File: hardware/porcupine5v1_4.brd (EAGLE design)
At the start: 28.5 x 29.7 mm, 45 parts, among them X1 PROGCON

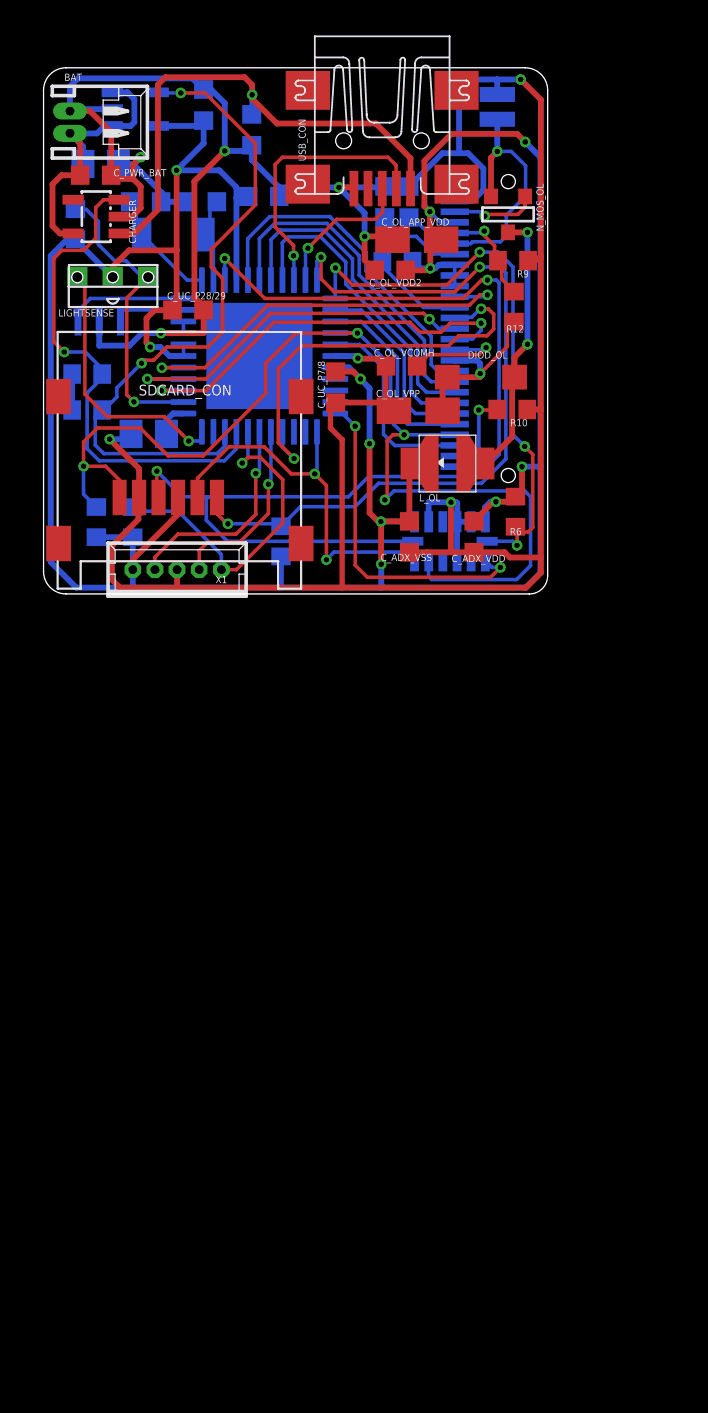
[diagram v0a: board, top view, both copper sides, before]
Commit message: added new OLEDdisplay
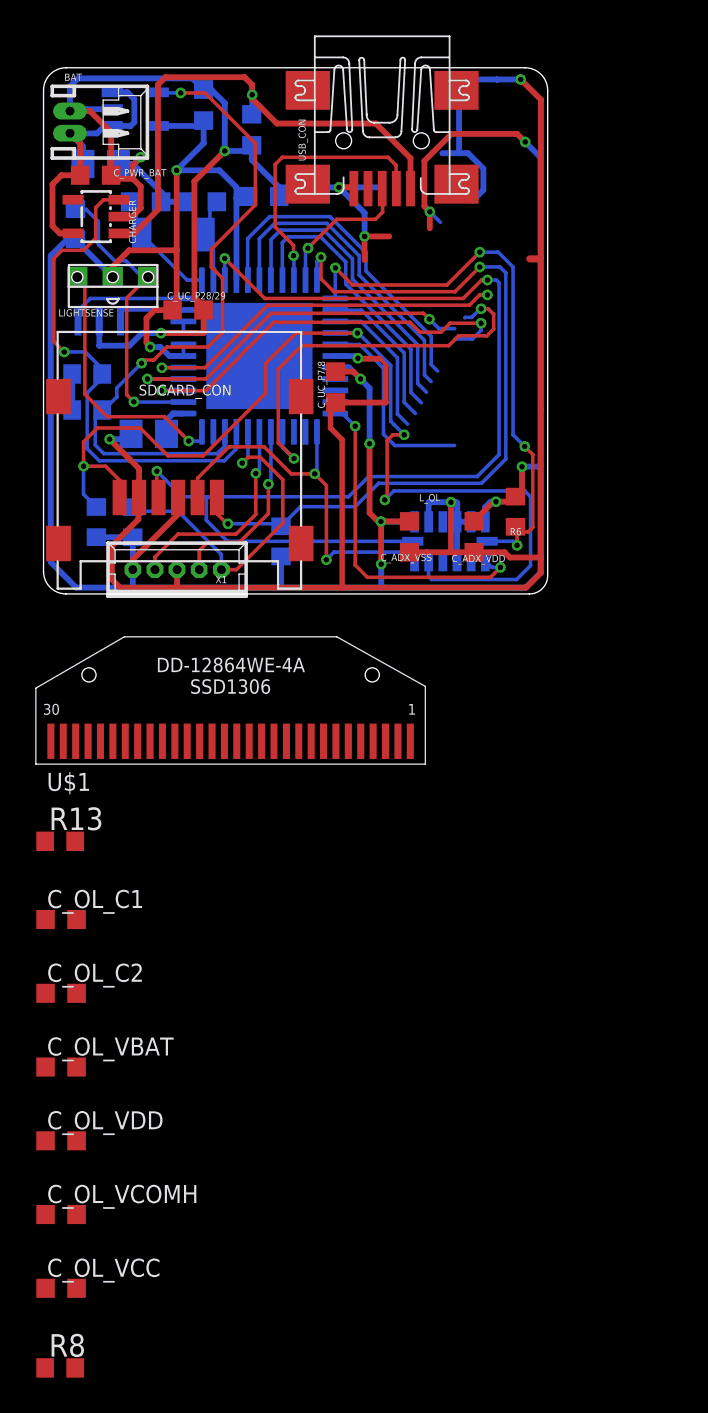
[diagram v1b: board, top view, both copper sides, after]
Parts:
- removed CON_OLED: OLED_DENSITRON, HedgehogLib:CON_DD-12864WE-1A
- removed C_OL_APP_VDD: 10µF/6.3V low ESR, rcl:A/3216-18R
- removed C_OL_FB: 1n, rcl:C0603K
- removed C_OL_VBREF: 1u, rcl:C0603K
- removed C_OL_VDD2: 1µF/16V, rcl:C0603K
- removed C_OL_VPP: 6.8µF/16V low ESR, rcl:A/3216-18R
- removed DIOD_OL: MBR0520, HedgehogLib:SOD123
- removed L_OL: 10µH, HedgehogLib:1212_FOR_INDUCTANCE
- removed N_MOS_OL: (no value), HedgehogLib:SOT-23
- removed R10: 820k, rcl:R0603
- removed R11, R12: 930k 1%, rcl:R0603
- removed R9: 110k 1%, rcl:R0603
- added C_OL_C1, C_OL_C2, C_OL_VBAT, C_OL_VDD: 1µF, rcl:C0603K
- added C_OL_VCC: 4.7µF, rcl:C0603K
- added R13: 400k, rcl:R0603
- added U$1: DD-12864WE-4A, HedgehogLib:CON_DD-12864WE-4A
- C_OL_VCOMH: value 4.7u -> 4.7µF
- R8: value 0.12 1% 0.5W -> 10k; device HedgehogLib:0805_UPSIDEDOWN -> rcl:R0603
- moved R8 75.4 mm to (0.94, -43.7), flipped to the top
- moved C_OL_VCOMH 51.6 mm to (0.99, -35.1)
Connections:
- removed net N$10: DIOD_OL.A, L_OL.P$2, N_MOS_OL.1
- removed net OL_FB: CON_OLED.P5, C_OL_FB.1, R12.1, R9.2
- removed net OL_IREF: CON_OLED.P26, R10.2
- removed net OL_SENSE: CON_OLED.P6, N_MOS_OL.2, R8.P$3
- removed net OL_SW: CON_OLED.P3, N_MOS_OL.3
- removed net OL_VBREF: CON_OLED.P7, C_OL_VBREF.1
- removed net OL_VCOMH: CON_OLED.P16, C_OL_VCOMH.2
- removed net OL_VPP_12V: CON_OLED.P17, C_OL_VPP.+, DIOD_OL.C, R12.2
- new net C1N: C_OL_C1.1, U$1.5
- new net C1P: C_OL_C1.2, U$1.4
- new net C2N: C_OL_C2.1, U$1.3
- new net C2P: C_OL_C2.2, U$1.2
- new net D/C#_OLED@RB5: U$1.15
- new net VCC: C_OL_VCC.1, U$1.28
- new net VCOMH: C_OL_VCOMH.1, U$1.27
- net +3V3: now also C_OL_VDD.1, R8.2, U$1.11, U$1.12, U$1.9; no longer CON_OLED.P10, CON_OLED.P4, CON_OLED.P8, CON_OLED.P9, C_OL_APP_VDD.+, C_OL_VDD2.2, L_OL.P$1, R11.2
- net A0_OLED@RB5: no longer CON_OLED.P13
- net CS_OLED@RE2: now also U$1.13; no longer CON_OLED.P11
- net D0_OLED@RD0: now also U$1.18; no longer CON_OLED.P18
- net D1_OLED@RD1: now also U$1.19; no longer CON_OLED.P19
- net D2_OLED@RD2: now also U$1.20; no longer CON_OLED.P20
- net D3_OLED@RD3: now also U$1.21; no longer CON_OLED.P21
- net D4_OLED@RD4: now also U$1.22; no longer CON_OLED.P22
- net D5_OLED@RD5: now also U$1.23; no longer CON_OLED.P23
- net D7_OLED@RD7: now also R13.2, U$1.25, U$1.26; no longer CON_OLED.P25
- net GND: now also C_OL_VBAT.2, C_OL_VCC.2, C_OL_VCOMH.2, C_OL_VDD.2, R13.1, U$1.1, U$1.10, U$1.29, U$1.30, U$1.8; no longer CON_OLED.P2, C_OL_APP_VDD.-, C_OL_FB.2, C_OL_VBREF.2, C_OL_VCOMH.1, C_OL_VDD2.1, C_OL_VPP.-, R10.1, R8.P$2, R9.1
- net RD_OLED@RE0: now also U$1.17; no longer CON_OLED.P15
- net RES_OLED: now also R8.1, U$1.14; no longer CON_OLED.P12, R11.1
- net SDO_SPI&D6_OLED@RD6: now also U$1.24; no longer CON_OLED.P24
- net V_BAT: now also C_OL_VBAT.1, U$1.6
- net WR_OLED@RE1: now also U$1.16; no longer CON_OLED.P14
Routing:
- net N$10: track 15.1 -> 0.00 mm, vias 2 -> 0
- net OL_SENSE: track 13.9 -> 0.00 mm, vias 1 -> 0
- net +3V3: track 176.7 -> 164.2 mm, vias 11 -> 10
- net OL_VPP_12V: track 10.1 -> 0.00 mm, vias 1 -> 0
- net GND: track 194.6 -> 185.2 mm
- net OL_FB: track 9.06 -> 0.00 mm, vias 1 -> 0
- net OL_VCOMH: track 6.15 -> 0.00 mm, vias 1 -> 0
- net OL_SW: track 5.36 -> 0.00 mm, vias 1 -> 0
- net RES_OLED: track 5.32 -> 0.00 mm
- net OL_VBREF: track 5.05 -> 0.00 mm
- net OL_IREF: track 4.80 -> 0.00 mm, vias 1 -> 0
- net SDO_SPI&D6_OLED@RD6: track 63.9 -> 61.0 mm
- net D5_OLED@RD5: track 11.0 -> 8.35 mm
- net D4_OLED@RD4: track 10.8 -> 8.58 mm
- net D3_OLED@RD3: track 18.0 -> 16.1 mm
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
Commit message: updated new OLED 5.1.4 version
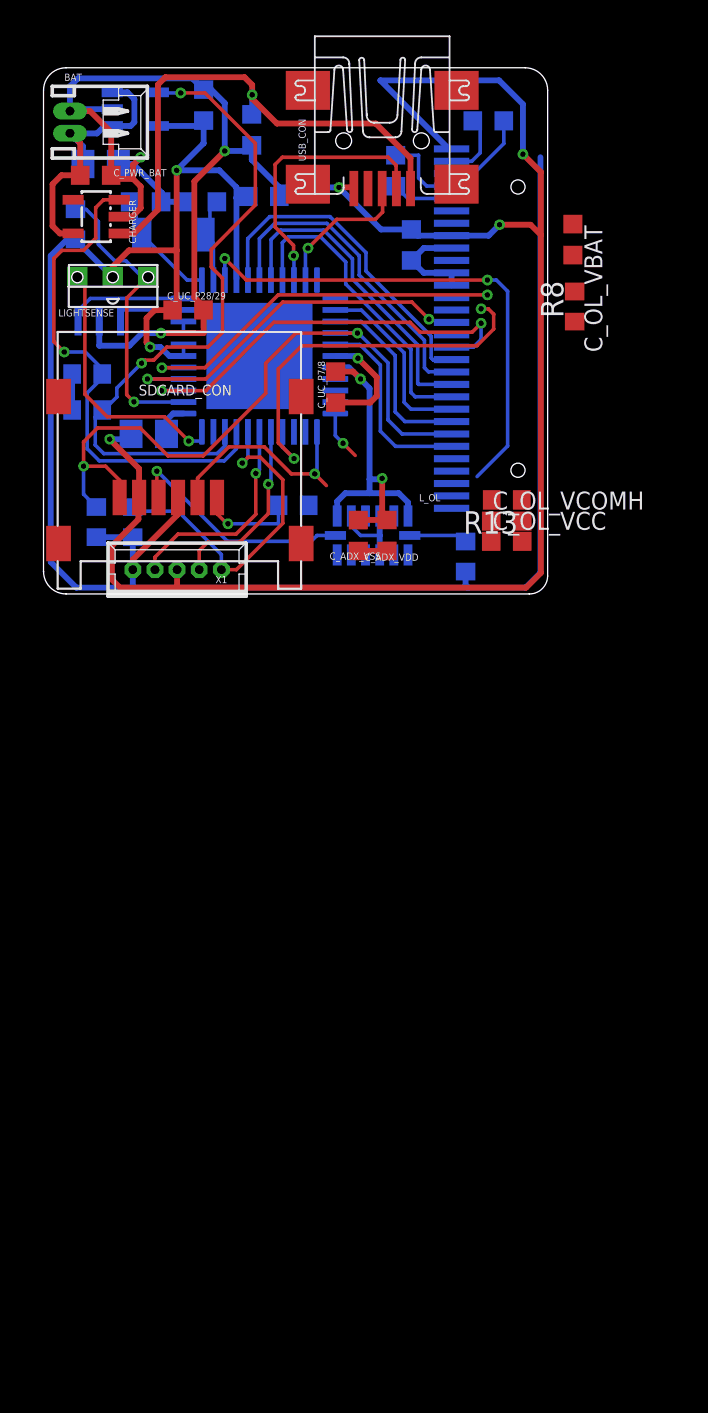
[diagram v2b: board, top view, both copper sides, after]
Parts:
- removed U$1: DD-12864WE-4A, HedgehogLib:CON_DD-12864WE-4A
- added OLED: DD-12864WE-4A, HedgehogLib:CON_DD-12864WE-4A
- moved R8 66.6 mm to (30.0, 16.2), turned to 90 degrees
- moved C_OL_VBAT 55.0 mm to (29.9, 20.0), turned to 270 degrees
- moved C_OL_C2 54.9 mm to (25.1, 26.7), flipped to the bottom
- moved C_OL_VDD 54.3 mm to (20.8, 19.7), flipped to the bottom, turned to 90 degrees
- moved C_OL_VCC 49.1 mm to (26.2, 2.97)
- moved C_OL_VCOMH 46.6 mm to (26.2, 4.11)
- moved C_OL_C1 46.3 mm to (19.9, 23.9), flipped to the bottom, turned to 90 degrees
- moved R13 31.7 mm to (26.2, 5.31), turned to 180 degrees
- moved C_ADX_VDD 4.91 mm to (19.4, 3.30)
- moved ACCERELOMETER 4.38 mm to (18.6, 3.30)
- moved R6 3.79 mm to (23.8, 2.11), flipped to the bottom, turned to 270 degrees
- moved C_ADX_VSS 2.89 mm to (17.8, 3.30)
- moved R4 2.16 mm to (14.1, 5.01), turned to 0 degrees
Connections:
- removed net A0_OLED@RB5: PIC_CONTROLLER.15
- new net IREF: OLED.26, R13.2
- net +3V3: now also OLED.11, OLED.12, OLED.9; no longer U$1.11, U$1.12, U$1.9
- net C1N: now also OLED.5; no longer U$1.5
- net C1P: now also OLED.4; no longer U$1.4
- net C2N: now also OLED.3; no longer U$1.3
- net C2P: now also OLED.2; no longer U$1.2
- net CS_ADX: now also PIC_CONTROLLER.9; no longer PIC_CONTROLLER.1
- net CS_OLED@RE2: now also OLED.13; no longer U$1.13
- net CS_SDCARD: now also PIC_CONTROLLER.10; no longer PIC_CONTROLLER.44
- net D/C#_OLED@RB5: now also OLED.15, PIC_CONTROLLER.15; no longer U$1.15
- net D0_OLED@RD0: now also OLED.18; no longer U$1.18
- net D1_OLED@RD1: now also OLED.19; no longer U$1.19
- net D2_OLED@RD2: now also OLED.20; no longer U$1.20
- net D3_OLED@RD3: now also OLED.21; no longer U$1.21
- net D4_OLED@RD4: now also OLED.22; no longer U$1.22
- net D5_OLED@RD5: now also OLED.23; no longer U$1.23
- net D7_OLED@RD7: now also OLED.25; no longer R13.2, U$1.25, U$1.26
- net GND: now also OLED.1, OLED.10, OLED.29, OLED.30, OLED.8; no longer U$1.1, U$1.10, U$1.29, U$1.30, U$1.8
- net RD_OLED@RE0: now also OLED.17; no longer U$1.17
- net RES_OLED: now also OLED.14; no longer U$1.14
- net SDO_SPI&D6_OLED@RD6: now also OLED.24; no longer U$1.24
- net VCC: now also OLED.28; no longer U$1.28
- net VCOMH: now also OLED.27; no longer U$1.27
- net V_BAT: now also OLED.6; no longer U$1.6
- net WR_OLED@RE1: now also OLED.16; no longer U$1.16
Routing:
- net CS_SDCARD: track 43.7 -> 5.67 mm, vias 3 -> 1
- net CS_ADX: track 32.7 -> 3.28 mm, vias 4 -> 0
- net A0_OLED@RB5: track 23.1 -> 0.00 mm, vias 2 -> 0
- net D/C#_OLED@RB5: track 0.00 -> 22.0 mm, vias 0 -> 2
- net SCLK: track 63.9 -> 42.5 mm
- net SDO_SPI&D6_OLED@RD6: track 61.0 -> 39.7 mm, vias 4 -> 2
- net GND: track 185.2 -> 167.4 mm, vias 9 -> 8
- net INT_ACC@RB2: track 19.0 -> 2.83 mm, vias 2 -> 1
- net +3V3: track 164.2 -> 150.4 mm, vias 10 -> 4
- net SDI: track 22.1 -> 12.4 mm, vias 2 -> 1
- net C2N: track 0.00 -> 4.94 mm
- net C1P: track 0.00 -> 4.63 mm
- net C2P: track 0.00 -> 3.79 mm
- net C1N: track 0.00 -> 3.44 mm
- net D5_OLED@RD5: track 8.35 -> 10.8 mm
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
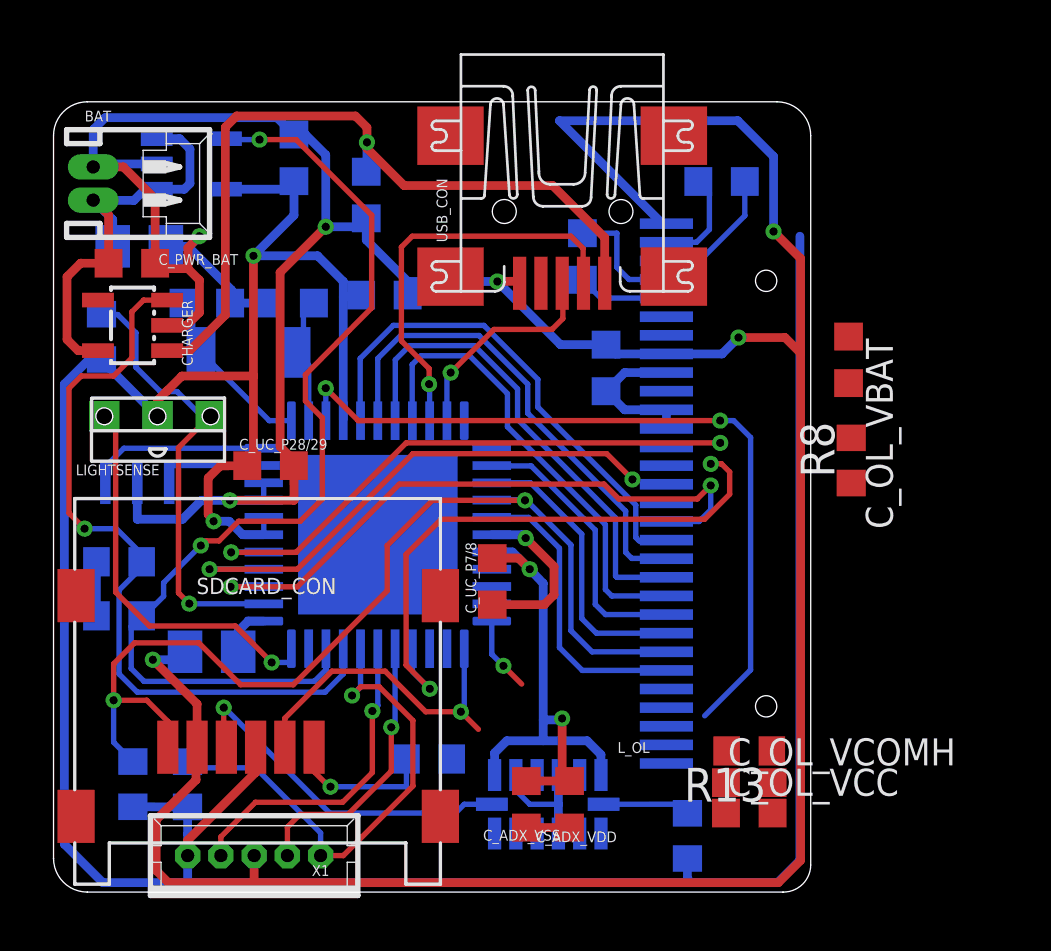
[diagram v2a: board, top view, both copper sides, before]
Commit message: updated OLED 5.1.4 version: wiring
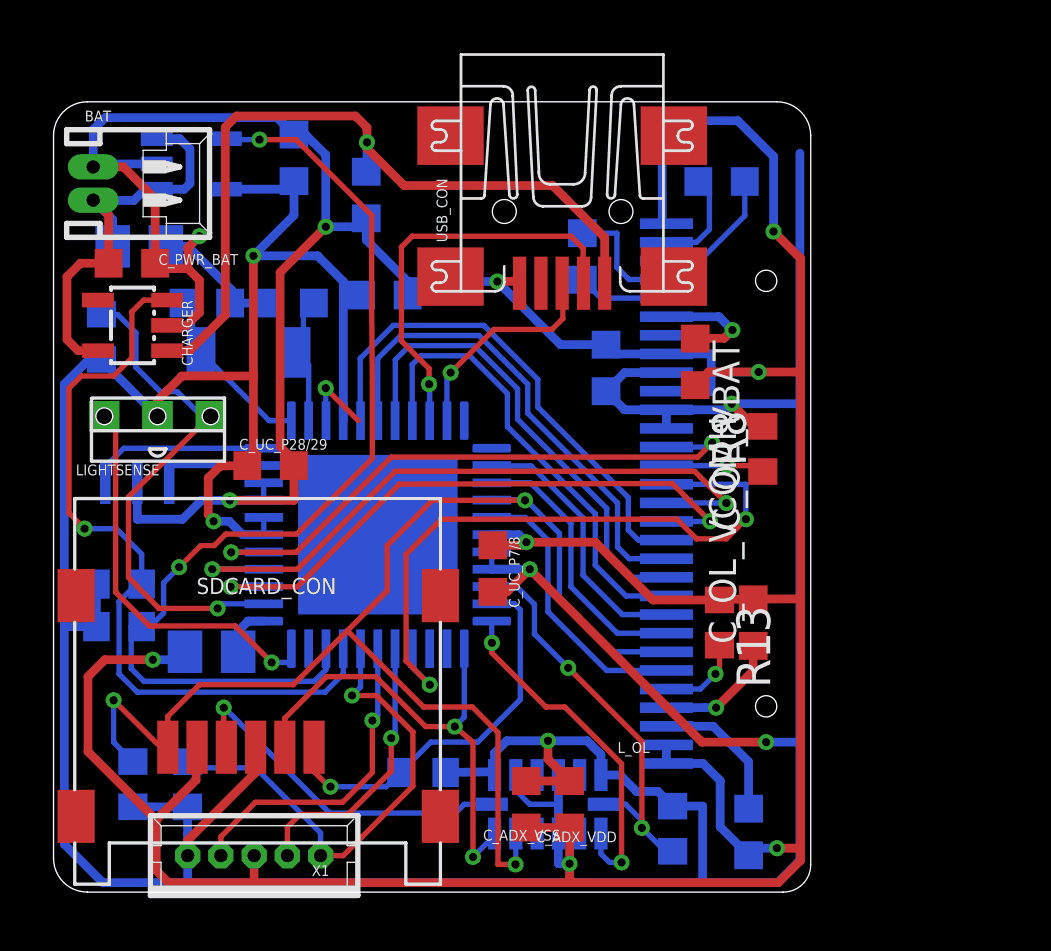
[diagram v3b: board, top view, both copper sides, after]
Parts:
- moved C_OL_VCOMH 6.02 mm to (26.3, 10.1), turned to 90 degrees
- moved C_OL_VBAT 5.77 mm to (24.1, 19.9)
- moved R13 4.95 mm to (25.0, 10.1), turned to 270 degrees
- moved R8 3.36 mm to (26.7, 16.7)
- moved R3 0.84 mm to (2.46, 11.6)
- moved C_OL_VCC 0.71 mm to (26.1, 2.26), flipped to the bottom, turned to 270 degrees
- moved R6 0.62 mm to (23.3, 2.38), turned to 90 degrees
- moved R4 0.56 mm to (13.9, 4.50)
- moved C_UC_P7/8 0.48 mm to (16.5, 12.2), turned to 90 degrees
- moved R5 0.41 mm to (2.46, 9.98)
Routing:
- net SCLK: track 42.5 -> 16.3 mm, vias 3 -> 2
- net GND: track 167.4 -> 191.7 mm, vias 8 -> 10
- net +3V3: track 150.4 -> 172.6 mm, vias 4 -> 6
- net CS_ADX: track 3.28 -> 15.4 mm, vias 0 -> 2
- net INT_ACC@RB2: track 2.83 -> 13.2 mm, vias 1 -> 2
- net SDO_SPI&D6_OLED@RD6: track 39.7 -> 50.0 mm, vias 2 -> 3
- net CS_SDCARD: track 5.67 -> 14.8 mm
- net SDI: track 12.4 -> 18.4 mm, vias 1 -> 2
- net VCC: track 0.00 -> 5.41 mm
- net WR_OLED@RE1: track 20.1 -> 25.5 mm
- net VCOMH: track 0.00 -> 4.77 mm, vias 0 -> 1
- net V_BAT: track 16.7 -> 21.0 mm, vias 0 -> 1
- net RES_OLED: track 0.00 -> 3.82 mm, vias 0 -> 1
- net IREF: track 0.00 -> 3.22 mm, vias 0 -> 1
- net D/C#_OLED@RB5: track 22.0 -> 25.1 mm
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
